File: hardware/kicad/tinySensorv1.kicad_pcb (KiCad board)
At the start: 2 copper layers, 94 x 60 mm, 39 parts, among them J1 RADIO, J10 CR2032 socket, J11 AAA socket, J12 AA Socket, J13 RAW IN, J2 DCDC converter, J3 I2C Sensor (BME/BMP 280), J4 PWM out, J5 OneWire sensor, J6 ISP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

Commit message: fix: missing connections in analog
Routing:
- net /RESET: track 48.4 -> 54.9 mm
- net /SENSOR_VCC: track 42.1 -> 47.0 mm
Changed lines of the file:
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@@
     (thickness 1)
     (drawings 101)
-    (tracks 205)
+    (tracks 207)
     (zones 0)
     (modules 39)
@@
     (descr "Through hole straight pin header, 1x03, 2.54mm pitch, single row")
     (tags "Through hole pin header THT 1x03 2.54mm single row")
-    (fp_text reference J7 (at 0 -2.33 90) (layer F.SilkS)
+    (fp_text reference J7 (at 2.0828 0.0508 180) (layer F.SilkS)
       (effects (font (size 1 1) (thickness 0.15)))
     )
@@
   (segment (start 173.469653 74.591827) (end 173.469653 72.362413) (width 0.25) (layer F.Cu) (net 7))
   (segment (start 173.469653 72.362413) (end 173.904347 71.92772) (width 0.25) (layer F.Cu) (net 7))
+  (segment (start 162.06216 78.68412) (end 162.06216 85.18412) (width 0.25) (layer F.Cu) (net 7))
   (segment (start 192.21196 52.99964) (end 194.0306 51.181) (width 0.25) (layer F.Cu) (net 8))
   (segment (start 190.43396 52.99964) (end 192.21196 52.99964) (width 0.25) (layer F.Cu) (net 8))
@@
   (segment (start 154.54 60.21964) (end 155.92044 61.60008) (width 0.25) (layer B.Cu) (net 14))
   (segment (start 154.54 57.26) (end 154.54 60.21964) (width 0.25) (layer B.Cu) (net 14))
-  (segment (start 155.92044 61.60008) (end 158.10008 61.60008) (width 0.25) (layer B.Cu) (net 14))
   (segment (start 194.174361 69.825639) (end 194 70) (width 0.25) (layer B.Cu) (net 14))
   (segment (start 194.174361 60.575441) (end 194.174361 69.825639) (width 0.25) (layer B.Cu) (net 14))
@@
   (segment (start 190.951999 73.048001) (end 175.800001 73.048001) (width 0.25) (layer B.Cu) (net 14))
   (segment (start 194 70) (end 190.951999 73.048001) (width 0.25) (layer B.Cu) (net 14))
-  (segment (start 161.546759 60.617319) (end 162.67176 61.74232) (width 0.25) (layer B.Cu) (net 14))
-  (segment (start 159.082841 60.617319) (end 161.546759 60.617319) (width 0.25) (layer B.Cu) (net 14))
-  (segment (start 158.10008 61.60008) (end 159.082841 60.617319) (width 0.25) (layer B.Cu) (net 14))
   (segment (start 162.67176 61.74232) (end 163.05276 61.74232) (width 0.25) (layer B.Cu) (net 14))
   (segment (start 163.05276 61.74232) (end 163.91636 62.60592) (width 0.25) (layer B.Cu) (net 14))
@@
   (segment (start 170.045001 71.245001) (end 172.546999 71.245001) (width 0.25) (layer B.Cu) (net 14))
   (segment (start 168.92 70.12) (end 170.045001 71.245001) (width 0.25) (layer B.Cu) (net 14))
+  (segment (start 156.903201 60.617319) (end 155.92044 61.60008) (width 0.25) (layer B.Cu) (net 14))
+  (segment (start 161.546759 60.617319) (end 156.903201 60.617319) (width 0.25) (layer B.Cu) (net 14))
+  (segment (start 162.67176 61.74232) (end 161.546759 60.617319) (width 0.25) (layer B.Cu) (net 14))
   (segment (start 176.54 62.5) (end 176.54 66.54) (width 0.25) (layer B.Cu) (net 15) (status 10))
   (via (at 176.54 66.54) (size 0.8) (drill 0.4) (layers F.Cu B.Cu) (net 15))
@@
   (segment (start 186.58332 51.181) (end 185.78068 50.37836) (width 0.25) (layer F.Cu) (net 15))
   (segment (start 188.9506 51.181) (end 186.58332 51.181) (width 0.25) (layer F.Cu) (net 15))
+  (segment (start 176.54 60.95476) (end 174.17796 58.59272) (width 0.25) (layer B.Cu) (net 15))
+  (segment (start 176.54 62.5) (end 176.54 60.95476) (width 0.25) (layer B.Cu) (net 15))
   (segment (start 180.205001 71.245001) (end 179.08 70.12) (width 0.25) (layer B.Cu) (net 16))
   (segment (start 182.160001 71.245001) (end 180.205001 71.245001) (width 0.25) (layer B.Cu) (net 16))

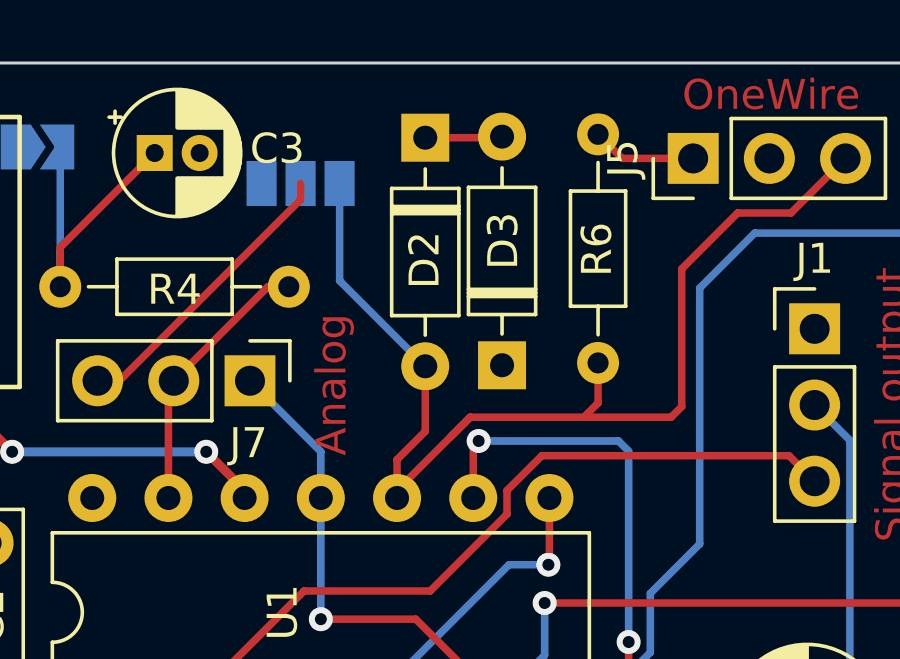
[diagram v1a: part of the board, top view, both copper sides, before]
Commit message: fix: missing connections in analog
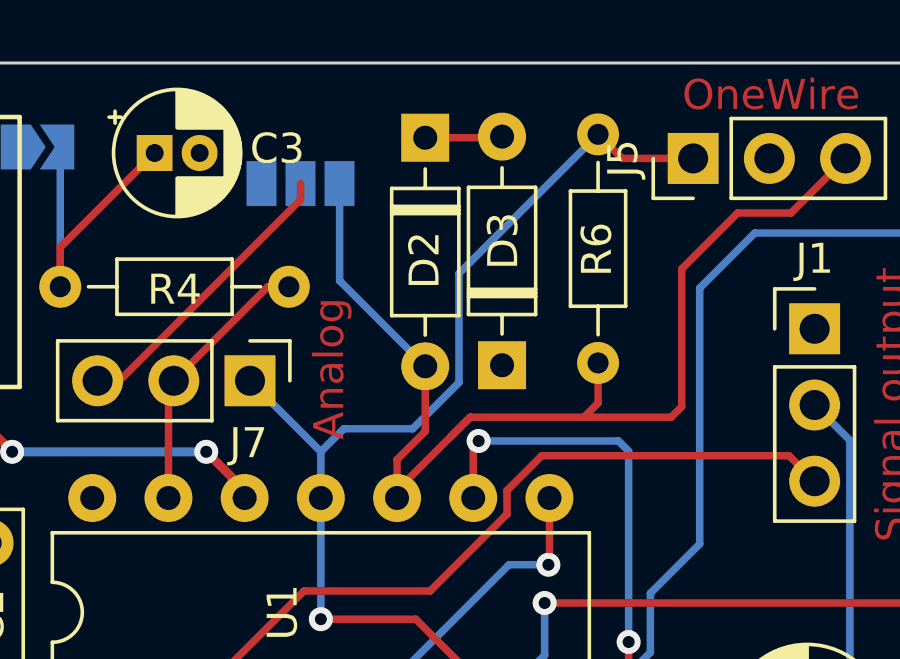
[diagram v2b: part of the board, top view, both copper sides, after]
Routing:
- net /SENSOR_VCC: track 47.0 -> 62.7 mm
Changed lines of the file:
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@@
     (thickness 1)
     (drawings 101)
-    (tracks 207)
+    (tracks 212)
     (zones 0)
     (modules 39)
@@
     (effects (font (size 1 1) (thickness 0.125)))
   )
-  (gr_text Analog (at 176.89576 58.71972 90) (layer F.Cu)
+  (gr_text Analog (at 176.81956 58.18632 90) (layer F.Cu)
     (effects (font (size 1 1) (thickness 0.125)))
   )
@@
   (segment (start 176.54 60.95476) (end 174.17796 58.59272) (width 0.25) (layer B.Cu) (net 15))
   (segment (start 176.54 62.5) (end 176.54 60.95476) (width 0.25) (layer B.Cu) (net 15))
+  (segment (start 181.144961 58.650121) (end 179.602162 60.19292) (width 0.25) (layer B.Cu) (net 15))
+  (segment (start 185.78068 50.37836) (end 181.144961 55.014079) (width 0.25) (layer B.Cu) (net 15))
+  (segment (start 181.144961 55.014079) (end 181.144961 58.650121) (width 0.25) (layer B.Cu) (net 15))
+  (segment (start 177.30184 60.19292) (end 176.54 60.95476) (width 0.25) (layer B.Cu) (net 15))
+  (segment (start 179.602162 60.19292) (end 177.30184 60.19292) (width 0.25) (layer B.Cu) (net 15))
   (segment (start 180.205001 71.245001) (end 179.08 70.12) (width 0.25) (layer B.Cu) (net 16))
   (segment (start 182.160001 71.245001) (end 180.205001 71.245001) (width 0.25) (layer B.Cu) (net 16))

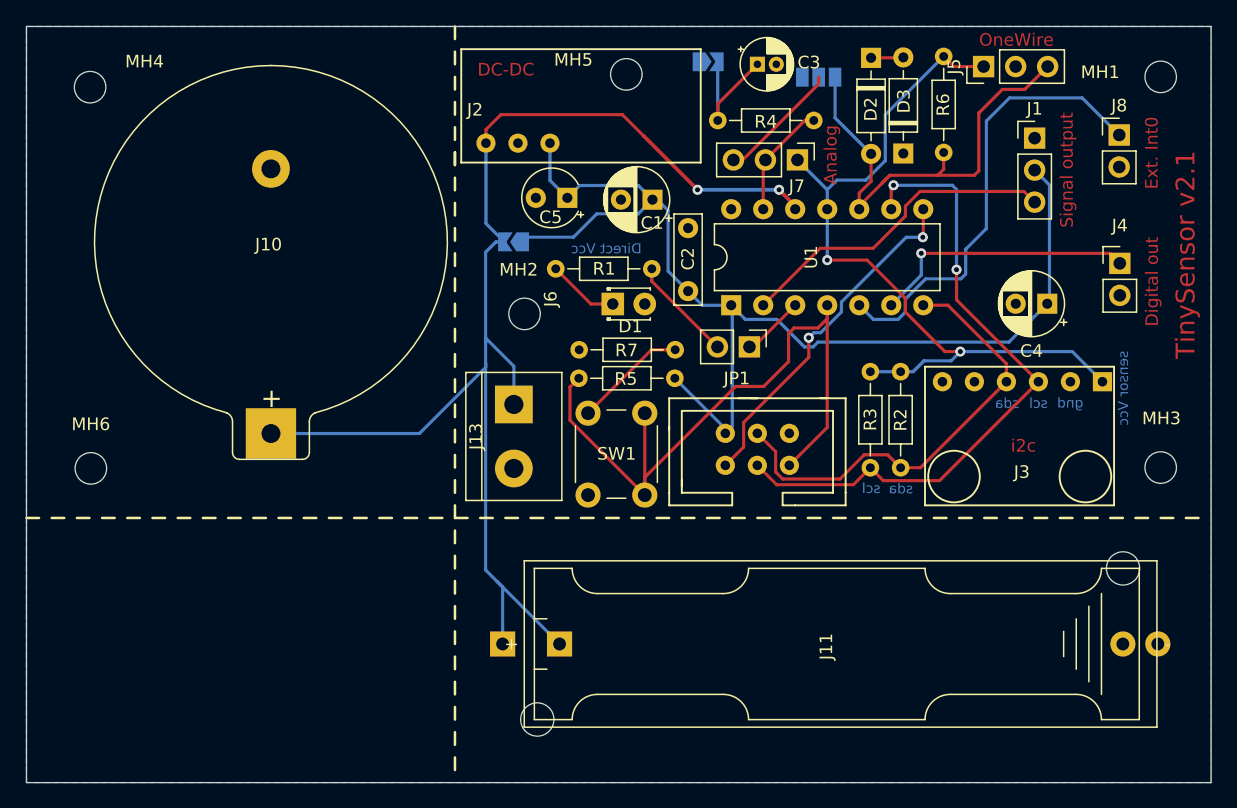
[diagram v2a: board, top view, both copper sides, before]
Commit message: fix: analog (LM35) documentation and layout
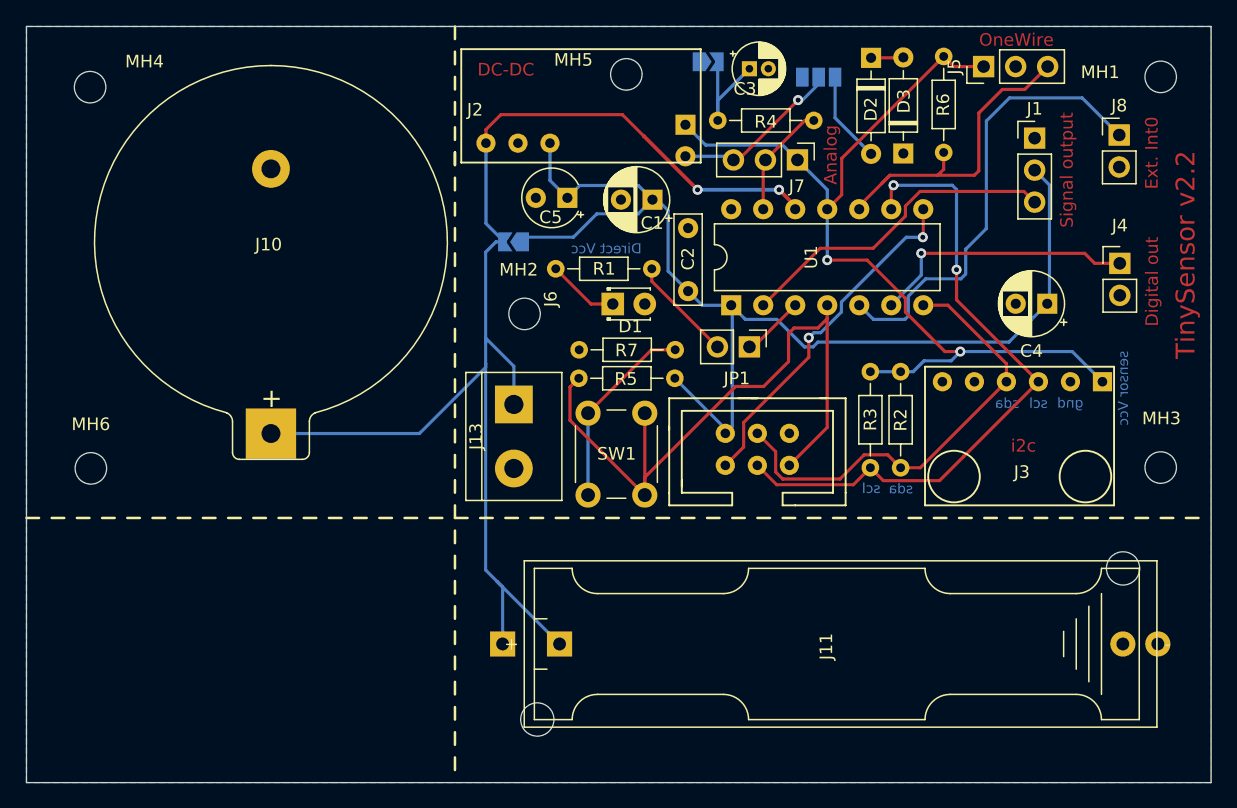
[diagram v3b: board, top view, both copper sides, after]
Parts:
- added C6: 0.1u, Capacitor_THT:CP_Radial_Tantal_D4.5mm_P2.50mm, B.Cu at (165.3, 55.8)
- moved C3 0.72 mm to (170.4, 51.4)
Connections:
- D2 pad 2: /OneWire -> Net-(D2-Pad2)
- JP4 pad 1: /OneWire -> Net-(D2-Pad2)
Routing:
- net /OneWire: track 37.4 -> 25.4 mm
- net /SENSOR_VCC: track 62.7 -> 73.0 mm
- net Net-(D2-Pad2): track 0.00 -> 7.27 mm
- net Net-(R7-Pad2): track 9.00 -> 15.5 mm
- net Net-(C6-Pad2): track 9.80 -> 14.5 mm, vias 0 -> 1
- net Net-(C3-Pad1): track 10.8 -> 10.1 mm
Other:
- board text added: "TinySensor v2.2"
- board text removed: "TinySensor v2.1"
